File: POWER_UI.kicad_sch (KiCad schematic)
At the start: 45 parts, among them J601 PWR_IN1, J602 PWR_IN2, J603 PWR_IN3, J604 PWR_IN4, J605 MCP_INT, J606 5V, J607 GND, J608 3V3, J609 EX_PA, J610 EX_PB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

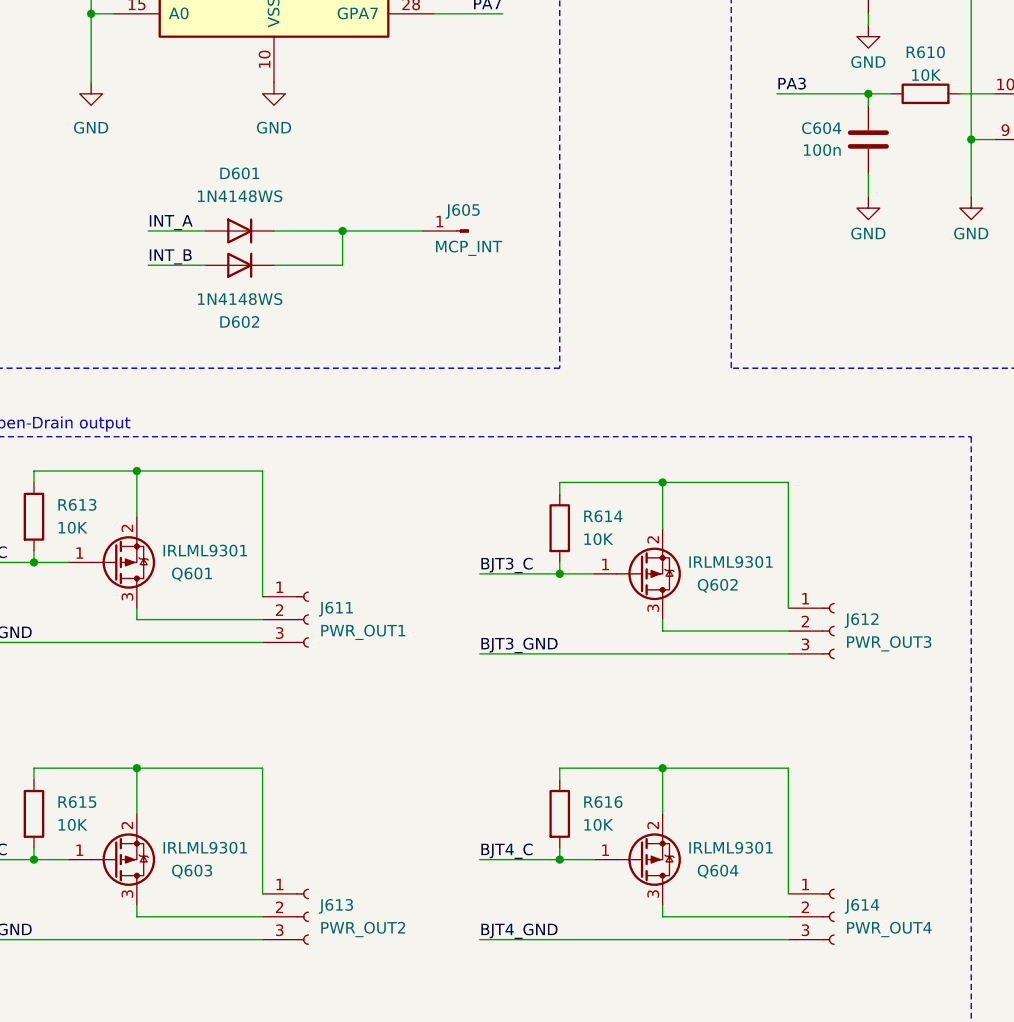
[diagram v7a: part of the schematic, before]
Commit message: added some lcsc codes, changed reverse voltage protection with a diode
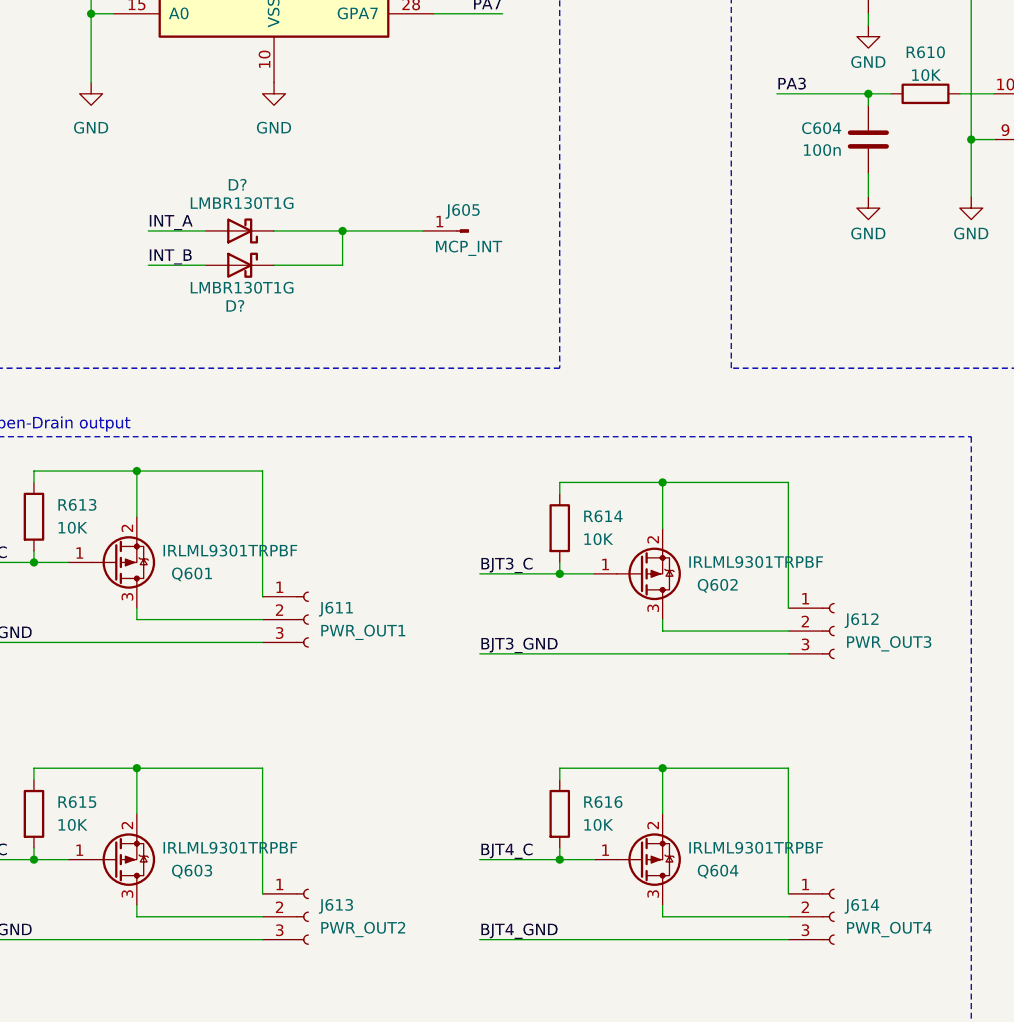
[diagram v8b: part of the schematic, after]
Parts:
- removed D601, D602: 1N4148WS, Diode_SMD:D_SOD-323_HandSoldering, symbol Diode:1N4148W
- added D? (x2): LMBR130T1G, Diode_SMD:D_SOD-123, symbol Device:D_Schottky
- JP601, JP602: footprint (none) -> Resistor_SMD:R_0603_1608Metric_Pad0.98x0.95mm_HandSolder; LCSC (none) -> C21189
- Q601, Q602, Q603, Q604: value IRLML9301 -> IRLML9301TRPBF; LCSC (none) -> C82056
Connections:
- net INT_A: now also D?.2 (A)
- net INT_B: now also D?.2 (A)
- net at J605.1 (Pin_1): now also D?.1 (K), D?.1 (K)
